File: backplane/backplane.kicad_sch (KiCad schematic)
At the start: 12 parts

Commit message: wip: backplane connectors
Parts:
- added CONECTOR_CCE_2: CONN_35X2, symbol CCE-2-rescue:CONN_35X2
- added CONECTOR_CT1_4: CONN_35X2, symbol CT1-4-rescue:CONN_35X2
- added CONECTOR_FIN_8: CONN_35X2, symbol FIN-8-rescue:CONN_35X2
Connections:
- net +(CAC+SOM): now also CONECTOR_CT1_4.4 (P4)
- net +AC_0: now also CONECTOR_FIN_8.49 (P49)
- net +AC_1: now also CONECTOR_FIN_8.50 (P50)
- net +AC_2: now also CONECTOR_FIN_8.51 (P51)
- net +AC_3: now also CONECTOR_FIN_8.52 (P52)
- net +AC_4: now also CONECTOR_FIN_8.53 (P53)
- net +AC_5: now also CONECTOR_FIN_8.54 (P54)
- net +AC_6: now also CONECTOR_FIN_8.55 (P55)
- net +AC_7: now also CONECTOR_FIN_8.56 (P56)
- net +ARA: now also CONECTOR_CT1_4.43 (P43)
- net +ATIVO: now also CONECTOR_CCE_2.2 (P2)
- net +CLOCK: now also CONECTOR_CCE_2.13 (P13)
- net +CS: now also CONECTOR_CCE_2.4 (P4)
- net +ESP-D: now also CONECTOR_CCE_2.10 (P10)
- net +E/A: now also CONECTOR_CT1_4.55 (P55)
- net +IME: now also CONECTOR_CT1_4.6 (P6)
- net +IMEADD: now also CONECTOR_CT1_4.41 (P41)
- net +IMENAND: now also CONECTOR_CT1_4.25
- net +IMEXOR: now also CONECTOR_CT1_4.44 (P44)
- net +INI: now also CONECTOR_CCE_2.29 (P29)
- net +IS: now also CONECTOR_CCE_2.3 (P3)
- net +MICG1: now also CONECTOR_CT1_4.39 (P39)
- net +MICRO: now also CONECTOR_CT1_4.22 (P22)
- net +PAR-D: now also CONECTOR_CCE_2.11 (P11)
- net +PER: now also CONECTOR_CCE_2.28 (P28)
- net +PUL: now also CONECTOR_CCE_2.30 (P30)
- net +RD_4: now also CONECTOR_CT1_4.52 (P52), CONECTOR_FIN_8.69 (P69)
- net +RD_5: now also CONECTOR_CT1_4.19 (P19), CONECTOR_FIN_8.34 (P34)
- net +RD_6: now also CONECTOR_CT1_4.53 (P53), CONECTOR_FIN_8.68 (P68)
- net +RD_7: now also CONECTOR_CT1_4.20 (P20), CONECTOR_FIN_8.33 (P33)
- net +RI_4: now also CONECTOR_FIN_8.31 (P31)
- net +RI_5: now also CONECTOR_CT1_4.10 (P10), CONECTOR_FIN_8.66 (P66)
- net +RI_6: now also CONECTOR_CT1_4.23 (P23), CONECTOR_FIN_8.32 (P32)
- net +RI_7: now also CONECTOR_FIN_8.67 (P67)
- net +RODA: now also CONECTOR_CCE_2.39 (P39)
- net +SAEDE: now also CONECTOR_CT1_4.54 (P54)
- net +SAEDS: now also CONECTOR_CT1_4.60 (P60)
- net +SHIFT: now also CONECTOR_CT1_4.42 (P42)
- net +SOM: now also CONECTOR_CT1_4.11 (P11)
- net +SUS: now also CONECTOR_CT1_4.45 (P45)
- net +T0: now also CONECTOR_CCE_2.14 (P14)
- net +T12: now also CONECTOR_CT1_4.12 (P12)
- net +T23: now also CONECTOR_CT1_4.46 (P46)
- net +T3: now also CONECTOR_CT1_4.50 (P50)
- net +T34: now also CONECTOR_CT1_4.40 (P40)
- net +T4: now also CONECTOR_CCE_2.16 (P16), CONECTOR_CT1_4.17 (P17), CONECTOR_FIN_8.28 (P28)
- net +T6: now also CONECTOR_CCE_2.31 (P31), CONECTOR_CT1_4.18 (P18), CONECTOR_FIN_8.29 (P29)
- net +T7: now also CONECTOR_CCE_2.18 (P18)
- net +TRI: now also CONECTOR_CT1_4.5 (P5)
- net +TRO: now also CONECTOR_CT1_4.62 (P62)
- net +Z/A: now also CONECTOR_CT1_4.7 (P7)
- net -CF1: now also CONECTOR_CCE_2.22 (P22)
- net -CF3: now also CONECTOR_CCE_2.24 (P24)
- net -CF4: now also CONECTOR_CCE_2.25
- net -CF5: now also CONECTOR_CCE_2.26 (P26)
- net -CLOCK: now also CONECTOR_CT1_4.16 (P16)
- net -F1: now also CONECTOR_CCE_2.41 (P41), CONECTOR_CT1_4.2 (P2)
- net -F2: now also CONECTOR_CCE_2.42 (P42), CONECTOR_CT1_4.37 (P37)
- net -F3: now also CONECTOR_CCE_2.43 (P43), CONECTOR_CT1_4.3 (P3)
- net -F4: now also CONECTOR_CCE_2.44 (P44), CONECTOR_CT1_4.38 (P38)
- net -F5: now also CONECTOR_CCE_2.45 (P45)
- net -INT: now also CONECTOR_CCE_2.54 (P54)
- net -LAL1: now also CONECTOR_CCE_2.37 (P37)
- net -PAR: now also CONECTOR_CCE_2.53 (P53)
- net -RDZ: now also CONECTOR_CT1_4.9 (P9)
- net -RODA: now also CONECTOR_CCE_2.46 (P46)
- net -SENTIDO: now also CONECTOR_FIN_8.6 (P6)
- net -SINTA: now also CONECTOR_FIN_8.10 (P10)
- net -T1: now also CONECTOR_CCE_2.19 (P19)
- net -T3: now also CONECTOR_CCE_2.21 (P21)
- net -T7: now also CONECTOR_CCE_2.20 (P20)
- net GND: now also CONECTOR_CCE_2.70 (P70), CONECTOR_CT1_4.70 (P70), CONECTOR_FIN_8.70 (P70)
- net MANEN: now also CONECTOR_FIN_8.65 (P65)
- net VCC: now also CONECTOR_CCE_2.1 (P1), CONECTOR_CT1_4.1 (P1), CONECTOR_FIN_8.1 (P1)
- new net +AC/X: CONECTOR_CT1_4.13 (P13)
- new net +C_AC: CONECTOR_CT1_4.21 (P21)
- new net +ESP: CONECTOR_CCE_2.49 (P49)
- new net +FN: CONECTOR_CCE_2.7 (P7)
- new net +MANDA: CONECTOR_CT1_4.61 (P61)
- new net +NAND: CONECTOR_CT1_4.26 (P26)
- new net +PAR: CONECTOR_CCE_2.48 (P48)
- new net +PARTIDA2: CONECTOR_CCE_2.51 (P51)
- new net +SOXOR: CONECTOR_CT1_4.59 (P59)
- new net +T45: CONECTOR_CT1_4.69 (P69)
- new net +T5: CONECTOR_CCE_2.17 (P17), CONECTOR_CT1_4.51 (P51)
- new net +T70: CONECTOR_CT1_4.15 (P15)
- new net +TR/T: CONECTOR_CT1_4.8 (P8)
- new net +TUBE: CONECTOR_FIN_8.8 (P8)
- new net +~{AC/X}: CONECTOR_CT1_4.57 (P57)
- new net -(BOT-ESP-A): CONECTOR_CCE_2.8 (P8)
- new net -(BOT-ESP-N): CONECTOR_CCE_2.9 (P9)
- new net -(BOT-PART-A): CONECTOR_CCE_2.5 (P5)
- new net -(BOT-PART-N): CONECTOR_CCE_2.6 (P6)
- new net -CF2: CONECTOR_CCE_2.23 (P23), CONECTOR_CT1_4.56 (P56)
- new net -COM_0: CONECTOR_FIN_8.60 (P60)
- new net -COM_1: CONECTOR_FIN_8.25
- new net -COM_10: CONECTOR_FIN_8.39 (P39)
- new net -COM_11: CONECTOR_FIN_8.4 (P4)
- new net -COM_12: CONECTOR_FIN_8.38 (P38)
- new net -COM_13: CONECTOR_FIN_8.3 (P3)
- new net -COM_14: CONECTOR_FIN_8.37 (P37)
- new net -COM_15: CONECTOR_FIN_8.2 (P2)
- new net -COM_2: CONECTOR_FIN_8.59 (P59)
- new net -COM_3: CONECTOR_FIN_8.24 (P24)
- new net -COM_4: CONECTOR_FIN_8.58 (P58)
- new net -COM_5: CONECTOR_FIN_8.23 (P23)
- new net -COM_6: CONECTOR_FIN_8.57 (P57)
- new net -COM_7: CONECTOR_FIN_8.22 (P22)
- new net -COM_8: CONECTOR_FIN_8.40 (P40)
- new net -COM_9: CONECTOR_FIN_8.5 (P5)
- new net -C_OVF: CONECTOR_CT1_4.24 (P24)
- new net -DADEN: CONECTOR_CT1_4.28 (P28)
- new net -DADSA: CONECTOR_CT1_4.27 (P27)
- new net -END_0: CONECTOR_FIN_8.62 (P62)
- new net -END_1: CONECTOR_FIN_8.27 (P27)
- new net -END_2: CONECTOR_FIN_8.61 (P61)
- new net -END_3: CONECTOR_FIN_8.26 (P26)
- new net -ESP: CONECTOR_CCE_2.52 (P52)
- new net -F1-D: CONECTOR_CCE_2.56 (P56)
- new net -F2-D: CONECTOR_CCE_2.57 (P57)
- new net -F3-D: CONECTOR_CCE_2.58 (P58)
- new net -F4-D: CONECTOR_CCE_2.59 (P59)
- new net -F5-D: CONECTOR_CCE_2.60 (P60)
- new net -FORÇA_PUG: CONECTOR_CCE_2.47 (P47)
- new net -LAL2: CONECTOR_CCE_2.38 (P38)
- new net -LAL4: CONECTOR_CCE_2.40 (P40)
- new net -PARTIDA2: CONECTOR_CCE_2.50 (P50)
- new net -PEDIDO_INTERRUPÇÃO: CONECTOR_CCE_2.27 (P27)
- new net -PED_INT: CONECTOR_FIN_8.7 (P7)
- new net -PED_INT_PAINEL: CONECTOR_FIN_8.9 (P9)
- new net -PRESET: CONECTOR_CCE_2.68 (P68)
- new net -T4*: CONECTOR_FIN_8.63 (P63)
- new net -T6*: CONECTOR_FIN_8.64 (P64)
- new net -XOR: CONECTOR_CT1_4.58 (P58)
- new net DAD_0: CONECTOR_FIN_8.14 (P14)
- new net DAD_1: CONECTOR_FIN_8.15 (P15)
- new net DAD_2: CONECTOR_FIN_8.16 (P16)
- new net DAD_3: CONECTOR_FIN_8.17 (P17)
- new net DAD_4: CONECTOR_FIN_8.18 (P18)
- new net DAD_5: CONECTOR_FIN_8.19 (P19)
- new net DAD_6: CONECTOR_FIN_8.20 (P20)
- new net DAD_7: CONECTOR_FIN_8.21 (P21)
- new net MANDA: CONECTOR_FIN_8.48 (P48)
- new net T/T: CONECTOR_CT1_4.68 (P68)
- new net pcb_15: CONECTOR_CCE_2.15 (P15)
- no-connect marks 216 -> 261
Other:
- note added: "(?)"
- note added: "PCP-2: PLACA CHAVES E PILOTO "Debounce" para chaves e drivers para lâmpadas piloto."
- note added: "PMR-1: PLACA MOSTRA REGISTRADORES Drivers para os LEDs."
- note added: "Placa CCE-2: Controle de estado."
- note added: "Placa CDE-3: Decodificador de instruções."
- note added: "Placa CRC-1: Relógio central."
- note added: "Placa CT1-4: Sinais de controle."
- note added: "Placa CT2-5: Sinais de controle."
- note added: "Placa CT3-6: Sinais de controle."
- note added: "Placa CT4-7: Sinais de controle."
- note added: "Placa CT5-8: Sinais de controle."
- note added: "Placa FCM-7: Interface com memória."
- note added: "Placa FIN-8: Sinais para cartões de interface."
- note added: "Placa FM1-6: Mais-um e porta de seleção 6."
- note removed: "Placa: * CDE-3 (decodificador de instruções)"
- note removed: "Placa: * CRC-1 (relógio central)"
- note removed: "Placa: * CT2-5 (sinais de controle)"
- note removed: "Placa: * CT3-6 (sinais de controle)"
- note removed: "Placa: * CT4-7 (sinais de controle)"
- note removed: "Placa: * CT5-8 (sinais de controle)"
- note removed: "Placa: * FCM-7 (interface com memória)"
- note removed: "Placa: * FM1-6 (mais-um e porta de seleção 6)"
- moved on the sheet: CONECTOR_FRONTAL_PMR_1, CONECTOR_TRASEIRO_PMR_1

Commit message: These are updated files after I loaded the project on a new version of KICAD
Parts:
- CONECTOR_FM1_6: footprint (none) -> Connector_DIN:DIN41612_C_3x32_Female_Vertical_THT

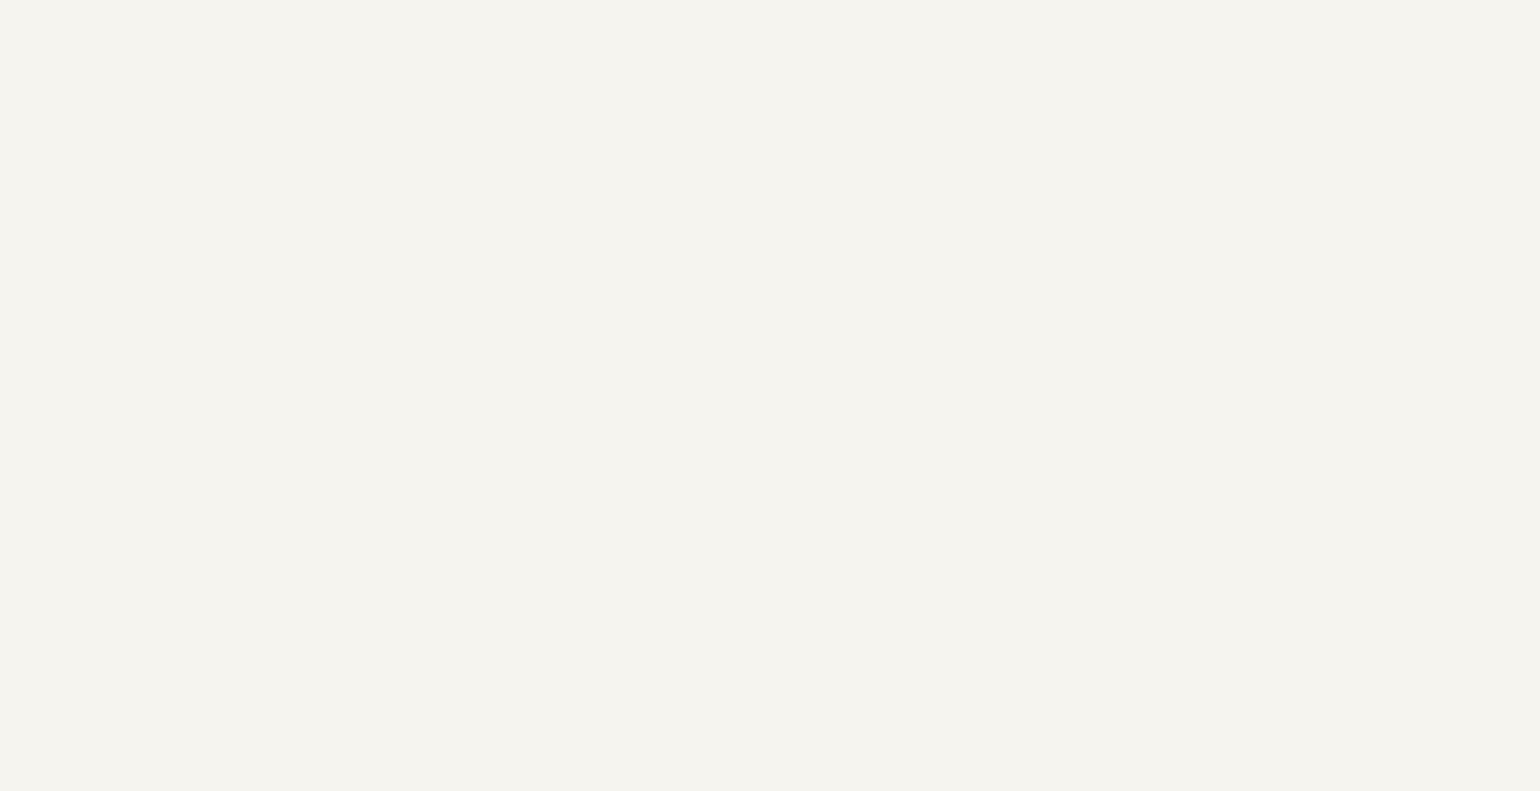
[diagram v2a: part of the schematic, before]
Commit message: add connectors for FS1_3 and FS2_4 to the backplane
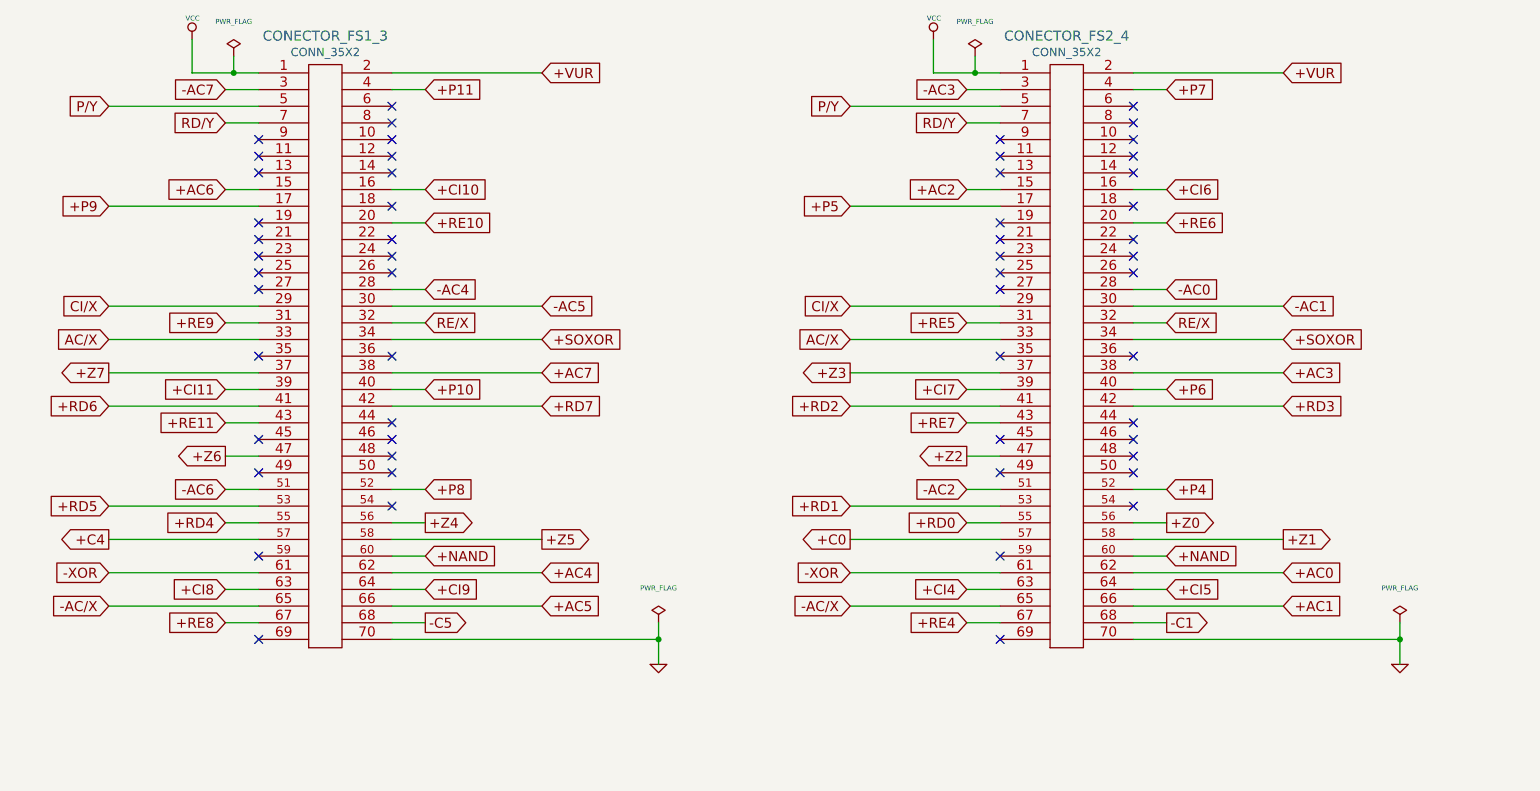
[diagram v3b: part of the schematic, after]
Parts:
- added CONECTOR_FS1_3, CONECTOR_FS2_4: CONN_35X2, symbol FS1-3-rescue:CONN_35X2-conn_35x2
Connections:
- net +NAND: now also CONECTOR_FS1_3.60 (P60), CONECTOR_FS2_4.60 (P60)
- net +SOXOR: now also CONECTOR_FS1_3.34 (P34), CONECTOR_FS2_4.34 (P34)
- net -C1: now also CONECTOR_FS2_4.68 (P68)
- net -XOR: now also CONECTOR_FS1_3.61 (P61), CONECTOR_FS2_4.61 (P61)
- net GND: now also CONECTOR_FS1_3.70 (P70), CONECTOR_FS2_4.70 (P70)
- net VCC: now also CONECTOR_FS1_3.1 (P1), CONECTOR_FS2_4.1 (P1)
- new net +AC0: CONECTOR_FS2_4.62 (P62)
- new net +AC1: CONECTOR_FS2_4.66 (P66)
- new net +AC2: CONECTOR_FS2_4.15 (P15)
- new net +AC3: CONECTOR_FS2_4.38 (P38)
- new net +AC4: CONECTOR_FS1_3.62 (P62)
- new net +AC5: CONECTOR_FS1_3.66 (P66)
- new net +AC6: CONECTOR_FS1_3.15 (P15)
- new net +AC7: CONECTOR_FS1_3.38 (P38)
- new net +C0: CONECTOR_FS2_4.57 (P57)
- new net +C4: CONECTOR_FS1_3.57 (P57)
- new net +CI10: CONECTOR_FS1_3.16 (P16)
- new net +CI11: CONECTOR_FS1_3.39 (P39)
- new net +CI4: CONECTOR_FS2_4.63 (P63)
- new net +CI5: CONECTOR_FS2_4.64 (P64)
- new net +CI6: CONECTOR_FS2_4.16 (P16)
- new net +CI7: CONECTOR_FS2_4.39 (P39)
- new net +CI8: CONECTOR_FS1_3.63 (P63)
- new net +CI9: CONECTOR_FS1_3.64 (P64)
- new net +P10: CONECTOR_FS1_3.40 (P40)
- new net +P11: CONECTOR_FS1_3.4 (P4)
- new net +P4: CONECTOR_FS2_4.52 (P52)
- new net +P5: CONECTOR_FS2_4.17 (P17)
- new net +P6: CONECTOR_FS2_4.40 (P40)
- new net +P7: CONECTOR_FS2_4.4 (P4)
- new net +P8: CONECTOR_FS1_3.52 (P52)
- new net +P9: CONECTOR_FS1_3.17 (P17)
- new net +RD0: CONECTOR_FS2_4.55 (P55)
- new net +RD1: CONECTOR_FS2_4.53 (P53)
- new net +RD2: CONECTOR_FS2_4.41 (P41)
- new net +RD3: CONECTOR_FS2_4.42 (P42)
- new net +RD4: CONECTOR_FS1_3.55 (P55)
- new net +RD5: CONECTOR_FS1_3.53 (P53)
- new net +RD6: CONECTOR_FS1_3.41 (P41)
- new net +RD7: CONECTOR_FS1_3.42 (P42)
- new net +RE10: CONECTOR_FS1_3.20 (P20)
- new net +RE11: CONECTOR_FS1_3.43 (P43)
- new net +RE4: CONECTOR_FS2_4.67 (P67)
- new net +RE5: CONECTOR_FS2_4.31 (P31)
- new net +RE6: CONECTOR_FS2_4.20 (P20)
- new net +RE7: CONECTOR_FS2_4.43 (P43)
- new net +RE8: CONECTOR_FS1_3.67 (P67)
- new net +RE9: CONECTOR_FS1_3.31 (P31)
- new net +VUR: CONECTOR_FS1_3.2 (P2), CONECTOR_FS2_4.2 (P2)
- new net +Z0: CONECTOR_FS2_4.56 (P56)
- new net +Z1: CONECTOR_FS2_4.58 (P58)
- new net +Z2: CONECTOR_FS2_4.47 (P47)
- new net +Z3: CONECTOR_FS2_4.37 (P37)
- new net +Z4: CONECTOR_FS1_3.56 (P56)
- new net +Z5: CONECTOR_FS1_3.58 (P58)
- new net +Z6: CONECTOR_FS1_3.47 (P47)
- new net +Z7: CONECTOR_FS1_3.37 (P37)
- new net -AC0: CONECTOR_FS2_4.28 (P28)
- new net -AC1: CONECTOR_FS2_4.30 (P30)
- new net -AC2: CONECTOR_FS2_4.51 (P51)
- new net -AC3: CONECTOR_FS2_4.3 (P3)
- new net -AC4: CONECTOR_FS1_3.28 (P28)
- new net -AC5: CONECTOR_FS1_3.30 (P30)
- new net -AC6: CONECTOR_FS1_3.51 (P51)
- new net -AC7: CONECTOR_FS1_3.3 (P3)
- new net -AC/X: CONECTOR_FS1_3.65 (P65), CONECTOR_FS2_4.65 (P65)
- new net -C5: CONECTOR_FS1_3.68 (P68)
- new net AC/X: CONECTOR_FS1_3.33 (P33), CONECTOR_FS2_4.33 (P33)
- new net CI/X: CONECTOR_FS1_3.29 (P29), CONECTOR_FS2_4.29 (P29)
- new net P/Y: CONECTOR_FS1_3.5 (P5), CONECTOR_FS2_4.5 (P5)
- new net RD/Y: CONECTOR_FS1_3.7 (P7), CONECTOR_FS2_4.7 (P7)
- new net RE/X: CONECTOR_FS1_3.32 (P32), CONECTOR_FS2_4.32 (P32)
- no-connect marks 261 -> 317

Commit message: FS1-3 + FS2-4
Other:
- moved on the sheet: CONECTOR_FS1_3, CONECTOR_FS2_4

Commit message: backplane
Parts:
- added CONECTOR_FR1_1, CONECTOR_FR2_2: CONN_35X2, symbol FR1-1-rescue:CONN_35X2-conn_35x2
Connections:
- net GND: now also CONECTOR_FR1_1.70 (P70), CONECTOR_FR2_2.70 (P70)
- net VCC: now also CONECTOR_FR1_1.1 (P1), CONECTOR_FR2_2.1 (P1)
- new net -I0: CONECTOR_FR1_1.38 (P38)
- new net -I1: CONECTOR_FR2_2.38 (P38)
- new net -I10: CONECTOR_FR1_1.11 (P11)
- new net -I11: CONECTOR_FR2_2.11 (P11)
- new net -I2: CONECTOR_FR1_1.3 (P3)
- new net -I3: CONECTOR_FR2_2.3 (P3)
- new net -I4: CONECTOR_FR1_1.48 (P48)
- new net -I5: CONECTOR_FR2_2.48 (P48)
- new net -I6: CONECTOR_FR1_1.47 (P47)
- new net -I7: CONECTOR_FR2_2.47 (P47)
- new net -I8: CONECTOR_FR1_1.9 (P9)
- new net -I9: CONECTOR_FR2_2.9 (P9)
- new net -R0: CONECTOR_FR1_1.33 (P33)
- new net -R0b: CONECTOR_FR1_1.69 (P69)
- new net -R1: CONECTOR_FR2_2.33 (P33)
- new net -R1b: CONECTOR_FR2_2.69 (P69)
- new net -R2: CONECTOR_FR1_1.62 (P62)
- new net -R2b: CONECTOR_FR1_1.68 (P68)
- new net -R3: CONECTOR_FR2_2.62 (P62)
- new net -R3b: CONECTOR_FR2_2.68 (P68)
- new net -R4: CONECTOR_FR1_1.32 (P32)
- new net -R4b: CONECTOR_FR1_1.50 (P50)
- new net -R5: CONECTOR_FR2_2.32 (P32)
- new net -R5b: CONECTOR_FR2_2.50 (P50)
- new net -R6: CONECTOR_FR1_1.30 (P30)
- new net -R6b: CONECTOR_FR1_1.19 (P19)
- new net -R7: CONECTOR_FR2_2.30 (P30)
- new net -R7b: CONECTOR_FR2_2.19 (P19)
- new net -RRE02468: CONECTOR_FR1_1.5 (P5)
- new net -RRE10: CONECTOR_FR1_1.44 (P44)
- new net -RRE11: CONECTOR_FR2_2.44 (P44)
- new net -RRE13579: CONECTOR_FR2_2.5 (P5)
- new net -SRE10: CONECTOR_FR1_1.43 (P43)
- new net -SRE11: CONECTOR_FR2_2.43 (P43)
- new net ??/I: CONECTOR_FR1_1.64 (P64), CONECTOR_FR2_2.64 (P64)
- new net C-CI: CONECTOR_FR1_1.34 (P34), CONECTOR_FR2_2.34 (P34)
- new net C-RD: CONECTOR_FR1_1.49 (P49), CONECTOR_FR2_2.49 (P49)
- new net C-RE: CONECTOR_FR1_1.40 (P40), CONECTOR_FR2_2.40 (P40)
- new net C-RI: CONECTOR_FR1_1.53 (P53), CONECTOR_FR2_2.53 (P53)
- new net CI0: CONECTOR_FR1_1.51 (P51)
- new net CI1: CONECTOR_FR2_2.51 (P51)
- new net CI10: CONECTOR_FR1_1.55 (P55)
- new net CI11: CONECTOR_FR2_2.55 (P55)
- new net CI2: CONECTOR_FR1_1.56 (P56)
- new net CI3: CONECTOR_FR2_2.56 (P56)
- new net CI4: CONECTOR_FR1_1.52 (P52)
- new net CI5: CONECTOR_FR2_2.52 (P52)
- new net CI6: CONECTOR_FR1_1.20 (P20)
- new net CI7: CONECTOR_FR2_2.20 (P20)
- new net CI8: CONECTOR_FR1_1.18 (P18)
- new net CI9: CONECTOR_FR2_2.18 (P18)
- new net CLEAR: CONECTOR_FR1_1.57 (P57), CONECTOR_FR2_2.57 (P57)
- new net L0: CONECTOR_FR1_1.24 (P24)
- new net L1: CONECTOR_FR2_2.24 (P24)
- new net L2: CONECTOR_FR1_1.60 (P60)
- new net L3: CONECTOR_FR2_2.60 (P60)
- new net L4: CONECTOR_FR1_1.27 (P27)
- new net L5: CONECTOR_FR2_2.27 (P27)
- new net L6: CONECTOR_FR1_1.29 (P29)
- new net L7: CONECTOR_FR2_2.29 (P29)
- new net L/R: CONECTOR_FR1_1.25, CONECTOR_FR2_2.25
- new net RD0: CONECTOR_FR1_1.14 (P14)
- new net RD1: CONECTOR_FR2_2.14 (P14)
- new net RD2: CONECTOR_FR1_1.54 (P54)
- new net RD3: CONECTOR_FR2_2.54 (P54)
- new net RD4: CONECTOR_FR1_1.15 (P15)
- new net RD5: CONECTOR_FR2_2.15 (P15)
- new net RD6: CONECTOR_FR1_1.21 (P21)
- new net RD7: CONECTOR_FR2_2.21 (P21)
- new net RE0: CONECTOR_FR1_1.37 (P37)
- new net RE1: CONECTOR_FR2_2.37 (P37)
- new net RE10: CONECTOR_FR1_1.42 (P42)
- new net RE11: CONECTOR_FR2_2.42 (P42)
- new net RE2: CONECTOR_FR1_1.2 (P2)
- new net RE3: CONECTOR_FR2_2.2 (P2)
- new net RE4: CONECTOR_FR1_1.13 (P13)
- new net RE5: CONECTOR_FR2_2.13 (P13)
- new net RE6: CONECTOR_FR1_1.12 (P12)
- new net RE7: CONECTOR_FR2_2.12 (P12)
- new net RE8: CONECTOR_FR1_1.7 (P7)
- new net RE9: CONECTOR_FR2_2.7 (P7)
- new net RE/I: CONECTOR_FR1_1.36 (P36), CONECTOR_FR2_2.36 (P36)
- new net RI0: CONECTOR_FR1_1.22 (P22)
- new net RI1: CONECTOR_FR2_2.22 (P22)
- new net RI2: CONECTOR_FR1_1.58 (P58)
- new net RI3: CONECTOR_FR2_2.58 (P58)
- new net RI4: CONECTOR_FR1_1.23 (P23)
- new net RI5: CONECTOR_FR2_2.23 (P23)
- new net RI6: CONECTOR_FR1_1.59 (P59)
- new net RI7: CONECTOR_FR2_2.59 (P59)
- new net U0: CONECTOR_FR1_1.4 (P4)
- new net U0_pino_63: CONECTOR_FR1_1.63 (P63)
- new net U1: CONECTOR_FR2_2.4 (P4)
- new net U1_pino_63: CONECTOR_FR2_2.63 (P63)
- new net U2: CONECTOR_FR1_1.46 (P46)
- new net U2_pino_66: CONECTOR_FR1_1.66 (P66)
- new net U3: CONECTOR_FR2_2.46 (P46)
- new net U3_pino_66: CONECTOR_FR2_2.66 (P66)
- new net U/R: CONECTOR_FR1_1.28 (P28), CONECTOR_FR2_2.28 (P28)
- new net Z0: CONECTOR_FR1_1.10 (P10)
- new net Z0_pino_65: CONECTOR_FR1_1.65 (P65)
- new net Z1: CONECTOR_FR2_2.10 (P10)
- new net Z1_pino_65: CONECTOR_FR2_2.65 (P65)
- new net Z2: CONECTOR_FR1_1.45 (P45)
- new net Z2_pino_61: CONECTOR_FR1_1.61 (P61)
- new net Z3: CONECTOR_FR2_2.45 (P45)
- new net Z3_pino_61: CONECTOR_FR2_2.61 (P61)
- new net Z4_pino_67: CONECTOR_FR1_1.67 (P67)
- new net Z5: CONECTOR_FR1_1.41 (P41), CONECTOR_FR2_2.41 (P41)
- new net Z5_pino_67: CONECTOR_FR2_2.67 (P67)
- new net Z6: CONECTOR_FR1_1.8 (P8)
- new net Z6_pino_31: CONECTOR_FR1_1.31 (P31)
- new net Z7: CONECTOR_FR2_2.8 (P8)
- new net Z7_pino_31: CONECTOR_FR2_2.31 (P31)
- new net Z/R: CONECTOR_FR1_1.26 (P26), CONECTOR_FR2_2.26 (P26)
- no-connect marks 317 -> 327
